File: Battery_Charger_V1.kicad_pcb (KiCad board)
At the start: 2 copper layers, 114.3 x 60.3 mm, 98 parts, among them J1 PJ-063AH, J2 Switch, J3 Pad, J4 Pad, J5 Pad, J6 Pad, Q1 IRF4905, Q2 IRF4905, Q3 PSMN4R2_40VSH, Q4 PSMN4R2_40VSH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

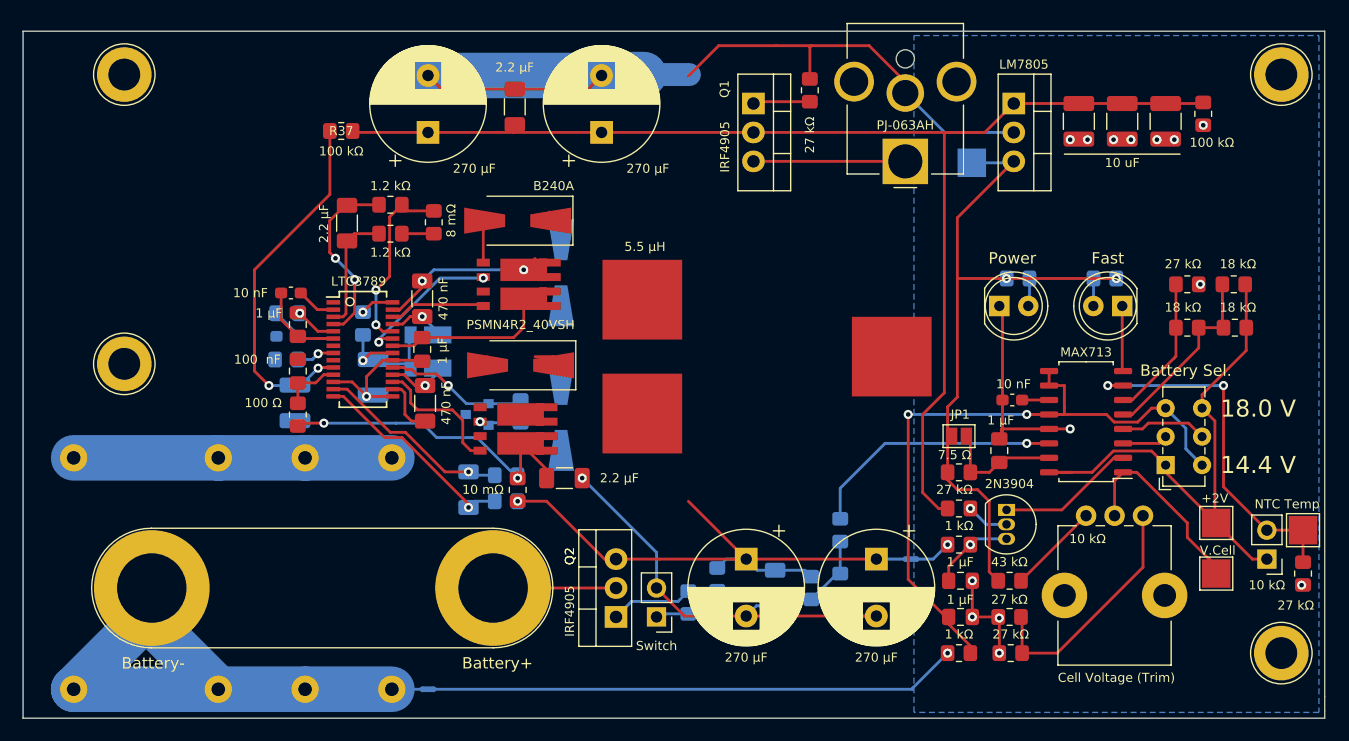
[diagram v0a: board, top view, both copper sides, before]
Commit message: Draft PCB(2)
Incomplete
Routing has begun to consider current associated with circuit traces.
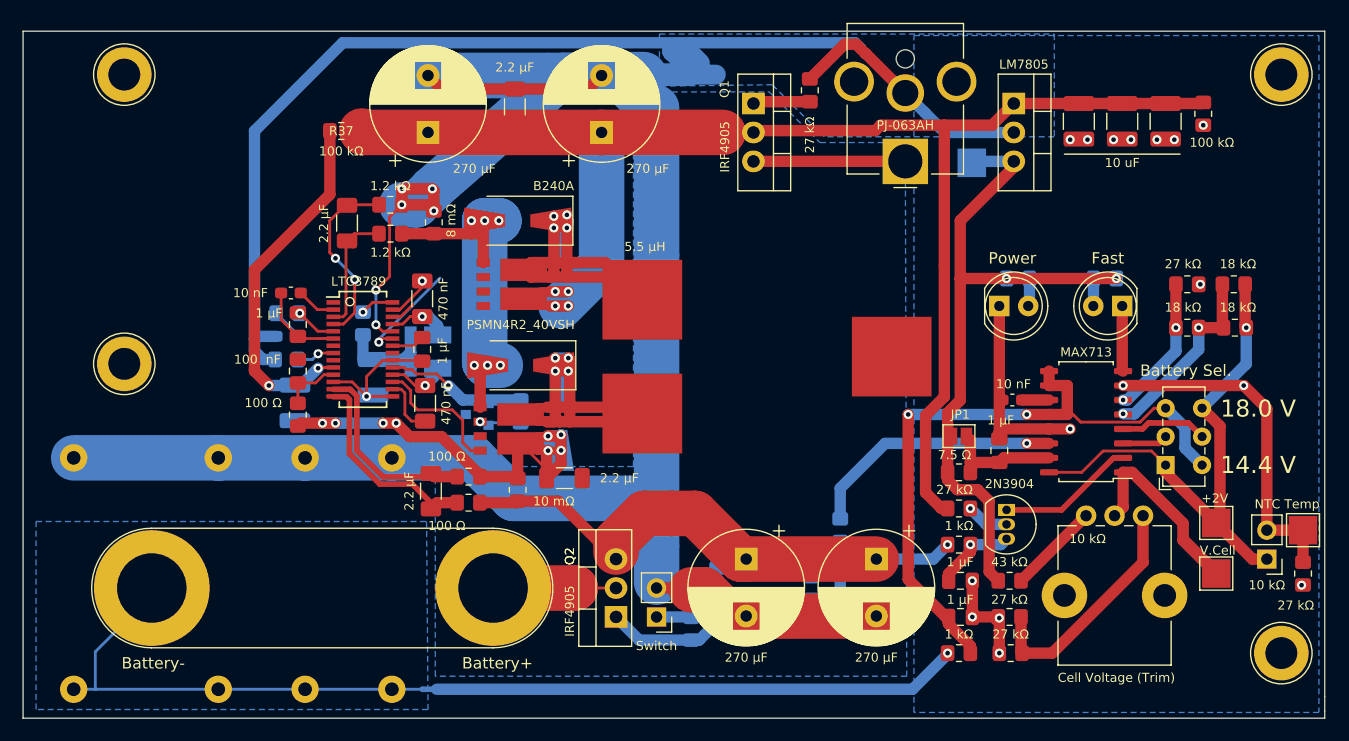
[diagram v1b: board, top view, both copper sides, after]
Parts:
- C14, R10, R11: moved to F.Cu
- moved R10 3.30 mm to (128.0, 112.9)
- moved R11 3.30 mm to (128.0, 115.2)
- moved C14 3.30 mm to (124.7, 114.2)
- moved R33 2.44 mm to (160.7, 124.9)
- moved R28 2.32 mm to (147.6, 126.3), turned to 270 degrees
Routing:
- net GNDPWR: track 147.4 -> 273.2 mm, vias 3 -> 6
- net GND: track 87.6 -> 181.5 mm
- net /DC: track 131.6 -> 182.6 mm, vias 0 -> 4
- net -BATT: track 92.8 -> 46.9 mm
- net Net-(NT3-Pad2): track 46.5 -> 88.3 mm
- net +5V: track 60.2 -> 97.7 mm
- net Net-(D7-Pad2): track 9.80 -> 45.5 mm, vias 0 -> 4
- net Net-(D6-Pad2): track 7.33 -> 38.0 mm, vias 0 -> 6
- net Net-(C5-Pad2): track 22.2 -> 50.9 mm, vias 2 -> 5
- net /VCELL: track 17.4 -> 30.1 mm
- net /Vout: track 34.7 -> 47.3 mm, vias 2 -> 8
- net Net-(C20-Pad1): track 32.8 -> 41.7 mm
- net Net-(D9-Pad2): track 12.2 -> 19.1 mm
- net /THI: track 16.9 -> 22.9 mm, vias 0 -> 2
- net Net-(Q3-Pad4): track 8.47 -> 2.41 mm
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- added copper zone on B.Cu, net -BATT
- added copper zone on B.Cu, net GNDPWR
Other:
- net class 0.25_mm added: clearance 0.2, trace_width 0.25, via_dia 0.8, via_drill 0.4
- net class 0.5_mm added: clearance 0.15, trace_width 0.5, via_dia 0.8, via_drill 0.4
- net class 1.75_mm added: clearance 0.2, trace_width 1.75, via_dia 0.8, via_drill 0.4
- net class 1_mm added: clearance 0.2, trace_width 1, via_dia 0.8, via_drill 0.4
- net class 4_mm: clearance 0.5 -> 0.2

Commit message: Draft PCB(3)
Pre-DRC
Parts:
- C1, C4, C8: moved to B.Cu
- moved C2 5.99 mm to (115.2, 95.5), turned to 180 degrees
- moved C4 3.45 mm to (115.1, 106.4), turned to 180 degrees
- moved R34 3.39 mm to (115.1, 101.1), turned to 0 degrees
- moved C20 3.21 mm to (114.6, 103.8), turned to 0 degrees
- moved C1 2.92 mm to (115.3, 97.2), turned to 180 degrees
- moved D3 2.75 mm to (121.9, 99.4), turned to 270 degrees
- moved C7 2.57 mm to (126.5, 102.1)
- moved C8 2.09 mm to (115.1, 99.1), turned to 180 degrees
- moved D4 2.05 mm to (122.7, 104.4), turned to 90 degrees
- moved C5 0.81 mm to (124.1, 98.1)
- moved R19 0.63 mm to (111.8, 98.0), turned to 90 degrees
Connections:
- R16 pad 2: /Vfb -> /V_FB
- R33 pad 1: /Vfb -> /V_FB
- R36 pad 2: /Vfb -> /V_FB
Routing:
- net /V_FB: track 0.00 -> 103.2 mm, vias 0 -> 9
- net /VSMPS: track 54.7 -> 103.6 mm
- net Net-(D6-Pad2): track 38.0 -> 69.5 mm, vias 6 -> 9
- net Net-(C20-Pad1): track 41.7 -> 27.4 mm, vias 2 -> 1
- net Net-(J1-Pad1): track 13.3 -> 26.8 mm
- net Net-(C5-Pad2): track 50.9 -> 63.0 mm, vias 5 -> 4
- net /Vfb: track 8.14 -> 0.00 mm
- net GNDPWR: track 273.2 -> 281.0 mm, vias 6 -> 7
- net Net-(Q3-Pad4): track 2.41 -> 8.55 mm
- net /INTVCC: track 16.6 -> 21.0 mm, vias 0 -> 3
- net Net-(Q3-Pad2): track 9.54 -> 13.4 mm, vias 1 -> 4
- net +BATT: track 10.8 -> 14.4 mm
- net Net-(C13-Pad2): track 16.2 -> 18.2 mm, vias 2 -> 0
- net /DC: track 182.6 -> 184.4 mm
- net Net-(C8-Pad2): track 4.13 -> 5.82 mm
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- added copper zone on F.Cu, net /VSMPS
- added copper zone on B.Cu, net Net-(D6-Pad2)
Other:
- net class 0.5_mm: clearance 0.15 -> 0.1
- net class 1_mm: clearance 0.2 -> 0.15
- net class 2_mm added: clearance 0.2, trace_width 2, via_dia 0.8, via_drill 0.4
- net class 3_mm added: clearance 0.1, trace_width 3, via_dia 0.8, via_drill 0.4
- net class Temp added: clearance 0.1, trace_width 0.5, via_dia 0.8, via_drill 0.4

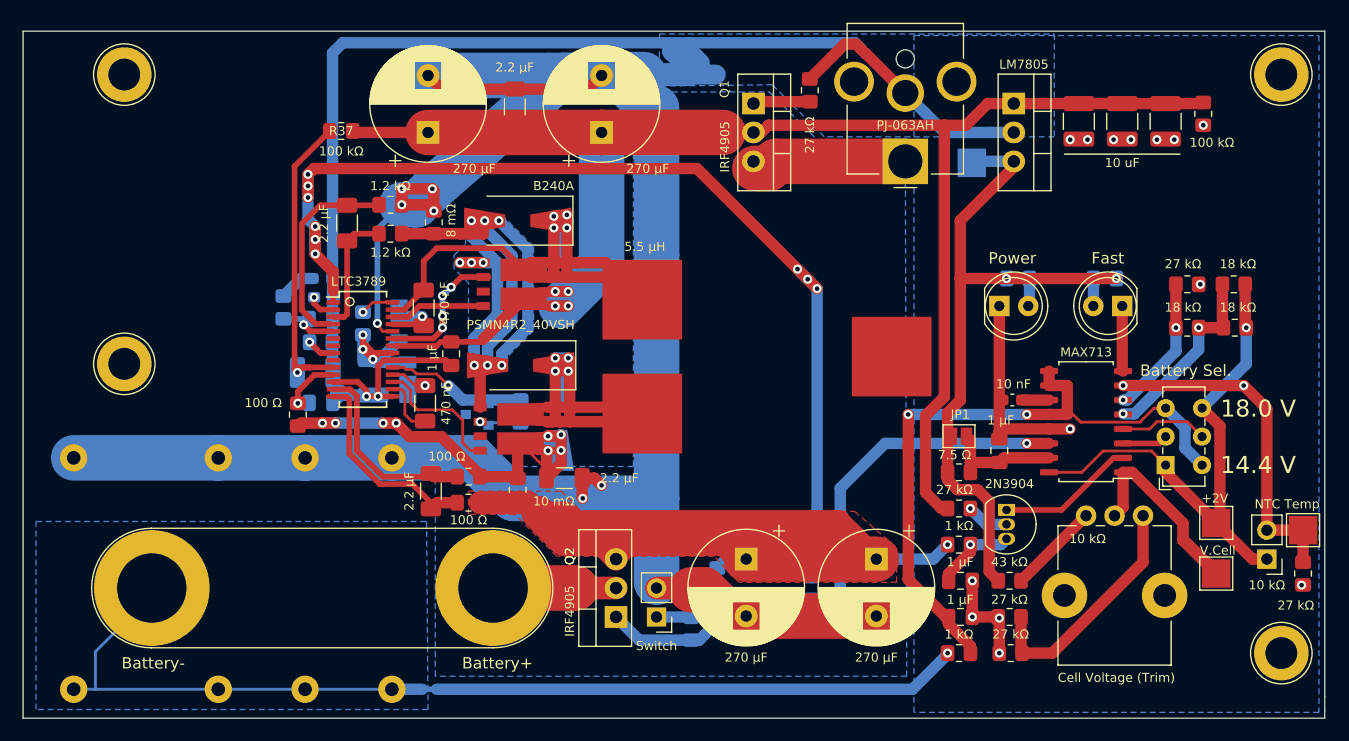
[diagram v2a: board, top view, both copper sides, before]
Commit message: Revised Switch Footprint
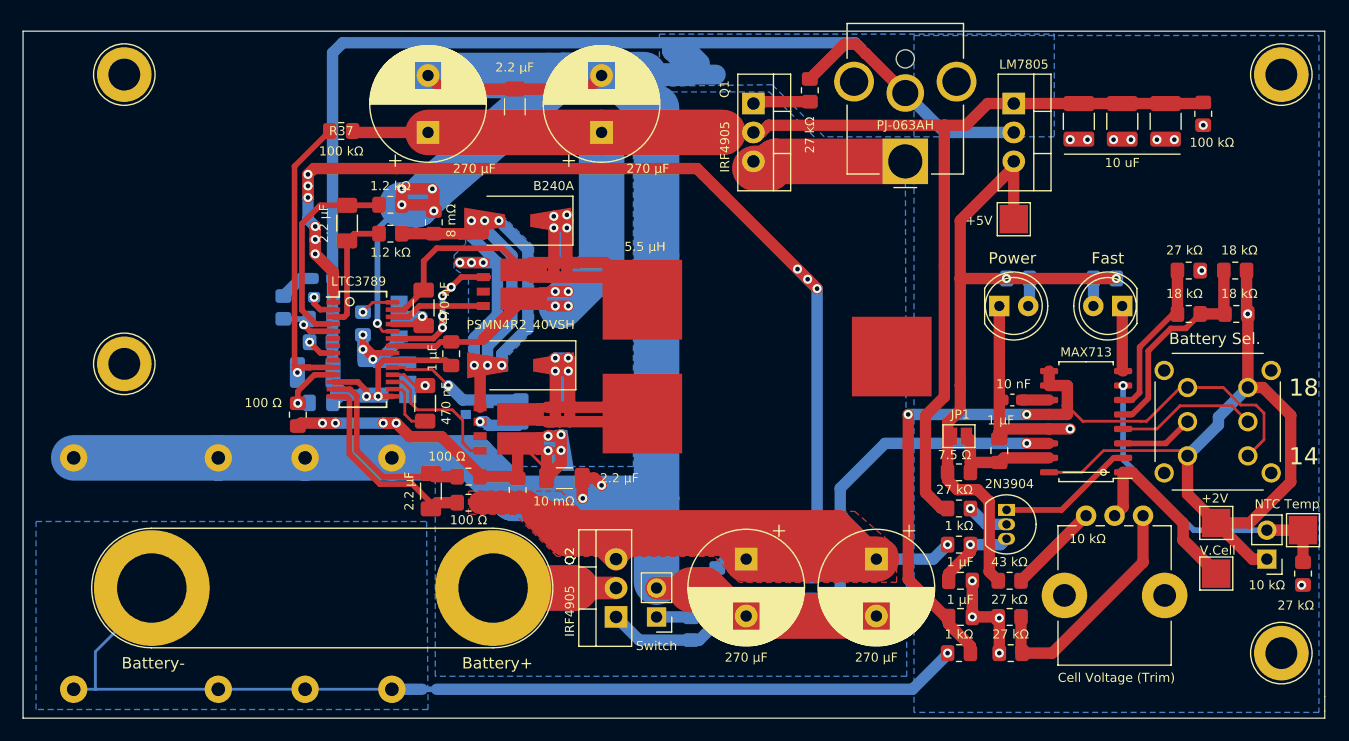
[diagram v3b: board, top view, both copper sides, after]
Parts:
- SW1: footprint Button_Switch_THT:SW_E-Switch_EG1271_DPDT -> CK_Switches:DPDT
- TP1: moved to F.Cu
- moved TP1 6.17 mm to (175.9, 90.3)
- moved SW1 5.95 mm to (193.8, 108.1), turned to 180 degrees
- moved R20 1.21 mm to (195.3, 94.8)
- moved R21 1.21 mm to (195.4, 98.6)
- moved R22 1.21 mm to (191.3, 98.6)
- moved R27 1.21 mm to (191.3, 94.8)
- moved D3 0.34 mm to (121.9, 99.1)
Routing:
- net +5V: track 97.7 -> 81.3 mm
- net /REF: track 48.5 -> 64.1 mm
- net /FB_BATT-: track 64.7 -> 72.6 mm
- net /PGM1: track 7.74 -> 12.4 mm
- net /BG2: track 3.47 -> 6.37 mm
- net /PGM0: track 3.98 -> 6.45 mm
- net /TEMP: track 30.1 -> 27.7 mm, vias 2 -> 1
- net /THI: track 22.9 -> 24.9 mm, vias 2 -> 0
- net /TLO: track 12.3 -> 14.0 mm, vias 2 -> 0
- net /Vout: track 47.3 -> 48.4 mm
- net Net-(Q3-Pad2): track 13.4 -> 14.5 mm
- net GND: track 181.3 -> 182.2 mm
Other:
- board text added: "14"
- board text added: "18"
- board text removed: "14.4 V"
- board text removed: "18.0 V"
